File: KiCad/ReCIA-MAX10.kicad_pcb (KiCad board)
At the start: 4 copper layers, 17.4 x 51.4 mm, 18 parts, among them J1 Conn_02x03_Odd_Even, U1 AMS1117-3.3, U2 SN74CBT16210, U3 SN74CBT16210, U4 10M02SCU169, U5 8520_DIP_SOCKET, X1 Oscillator_3.2x2.5mm-28.6363M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

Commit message: more routing, pin assignments and silkscreen fixes
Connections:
- net Net-(U3-Pad25) renamed PA2_3V3
- net Net-(U3-Pad26) renamed PA1_3V3
- net Net-(U3-Pad27) renamed PA0_3V3
- net Net-(U3-Pad28) renamed PA3_3V3
- net Net-(U3-Pad29) renamed PA4_3V3
- net Net-(U3-Pad30) renamed PA5_3V3
- net Net-(U3-Pad31) renamed PA6_3V3
- net Net-(U3-Pad33) renamed PA7_3V3
- net Net-(U3-Pad36) renamed D2_3V3
- net Net-(U3-Pad37) renamed D1_3V3
- net Net-(U3-Pad38) renamed D0_3V3
- net Net-(U3-Pad39) renamed RESET_3V3
- net Net-(U3-Pad40) renamed A3_3V3
- net Net-(U3-Pad42) renamed A2_3V3
- net Net-(U3-Pad43) renamed CNT_3V3
- net Net-(U3-Pad44) renamed SP_3V3
- net Net-(U3-Pad45) renamed A0_3V3
- net Net-(U3-Pad46) renamed A1_3V3
- U3 pad 10: Net-(U3-Pad10) -> D0
- U3 pad 11: Net-(U3-Pad11) -> D1
- U3 pad 12: Net-(U3-Pad12) -> D2
- U3 pad 6: Net-(U3-Pad6) -> A2
- U3 pad 7: Net-(U3-Pad7) -> A3
- U3 pad 9: Net-(U3-Pad9) -> RESET
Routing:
- net D2: track 0.00 -> 18.1 mm
- net D1: track 0.00 -> 15.4 mm
- net D0: track 0.00 -> 12.7 mm
- net D2_3V3: track 0.00 -> 12.5 mm, vias 0 -> 1
- net D1_3V3: track 0.00 -> 12.1 mm, vias 0 -> 1
- net D0_3V3: track 0.00 -> 11.4 mm, vias 0 -> 1
- net RESET: track 0.00 -> 10.0 mm
- net A3: track 0.00 -> 7.34 mm
- net A2: track 0.00 -> 6.55 mm
- net RESET_3V3: track 0.00 -> 3.07 mm
- net A3_3V3: track 0.00 -> 2.82 mm
- net GND: vias 56 -> 58
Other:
- board text added: "1A"
- board text added: "8520"
- board text added: "ReCIA"
- board text added: "Rev."

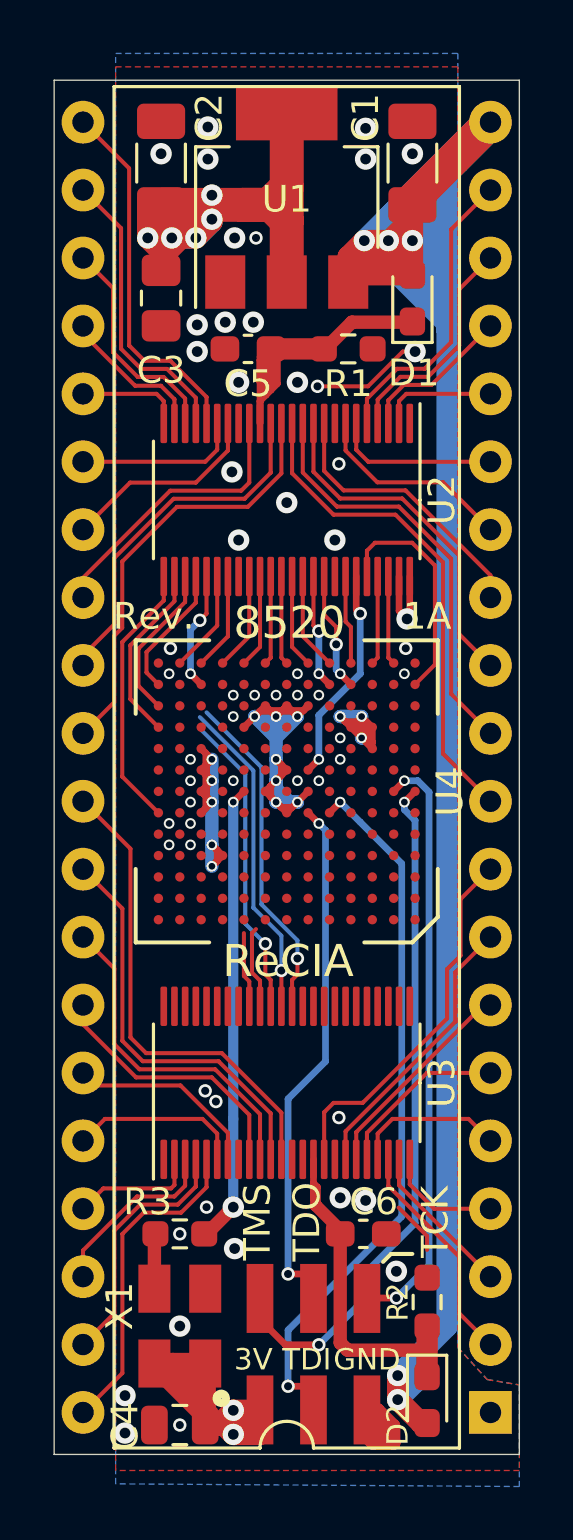
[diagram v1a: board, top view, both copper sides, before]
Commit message: more pin assignments and routing
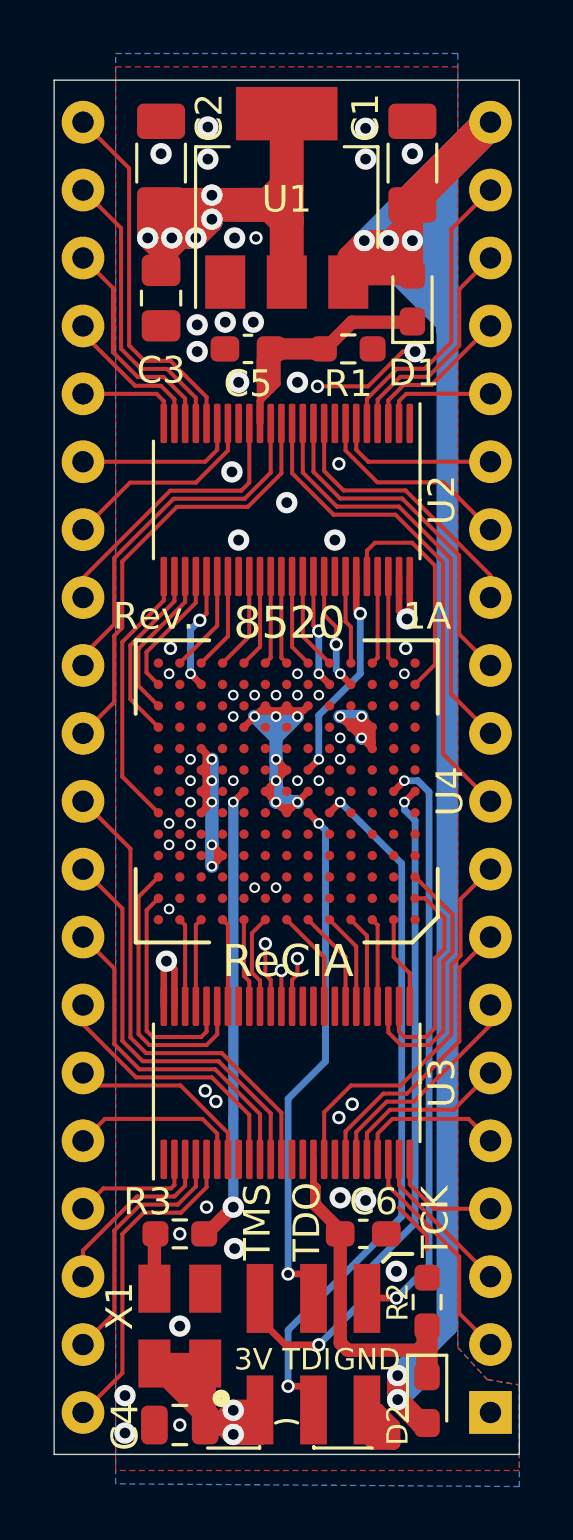
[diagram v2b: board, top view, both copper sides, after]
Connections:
- U3 pad 13: Net-(U3-Pad13) -> GND
- U3 pad 14: Net-(U3-Pad14) -> GND
- U4 pad A10: Net-(U4-PadA10) -> A2_3V3
- U4 pad A11: Net-(U4-PadA11) -> A0_3V3
- U4 pad A12: Net-(U4-PadA12) -> A1_3V3
- U4 pad A2: Net-(U4-PadA2) -> PA2_3V3
- U4 pad A3: Net-(U4-PadA3) -> PA3_3V3
- U4 pad A4: Net-(U4-PadA4) -> PA4_3V3
- U4 pad A5: Net-(U4-PadA5) -> PA5_3V3
- U4 pad A6: Net-(U4-PadA6) -> PA6_3V3
- U4 pad A7: Net-(U4-PadA7) -> PA7_3V3
- U4 pad A8: Net-(U4-PadA8) -> RESET_3V3
- U4 pad A9: Net-(U4-PadA9) -> A3_3V3
- U4 pad B1: Net-(U4-PadB1) -> PA1_3V3
- U4 pad B13: Net-(U4-PadB13) -> SP_3V3
- U4 pad C1: Net-(U4-PadC1) -> PA0_3V3
- U4 pad C13: Net-(U4-PadC13) -> CNT_3V3
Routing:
- net D1_3V3: track 12.1 -> 1.34 mm
- net D2_3V3: track 12.5 -> 1.87 mm
- net CNT_3V3: track 0.00 -> 10.5 mm
- net PA0_3V3: track 0.00 -> 9.93 mm
- net D0_3V3: track 11.4 -> 2.42 mm
- net SP_3V3: track 0.00 -> 8.50 mm
- net PA1_3V3: track 0.00 -> 8.18 mm
- net PA7_3V3: track 0.00 -> 3.82 mm
- net PA6_3V3: track 0.00 -> 3.82 mm
- net PA5_3V3: track 0.00 -> 3.65 mm
- net GND: track 15.8 -> 19.4 mm, vias 58 -> 63
- net PA4_3V3: track 0.00 -> 3.49 mm
- net PA2_3V3: track 0.00 -> 3.49 mm
- net PA3_3V3: track 0.00 -> 3.32 mm
- net A2_3V3: track 0.00 -> 3.32 mm
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
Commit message: more power routing, vias and silkscreen fixes
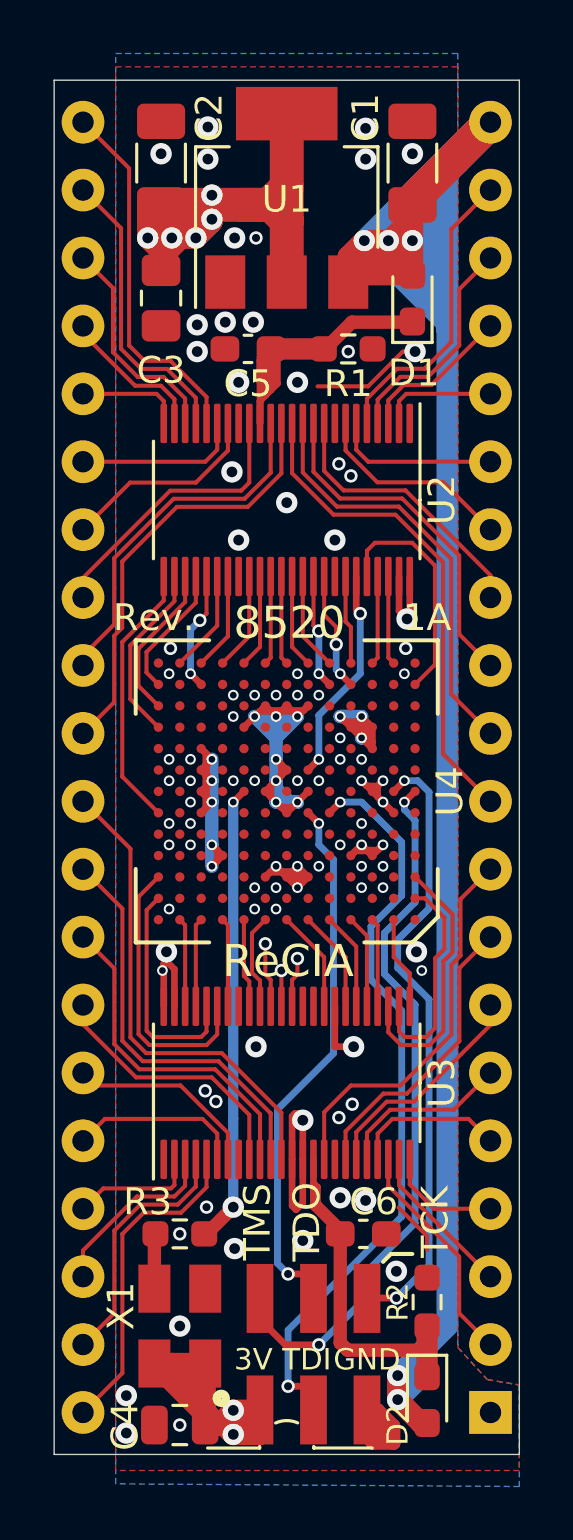
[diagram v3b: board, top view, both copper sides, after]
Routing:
- net 3V3: track 102.0 -> 116.7 mm, vias 22 -> 30
- net GND: track 19.4 -> 29.2 mm, vias 63 -> 84
- net TDI: track 26.9 -> 28.3 mm
- net TCK: track 22.2 -> 23.2 mm
- net TMS: track 25.9 -> 26.9 mm
- net TDO: track 19.9 -> 20.5 mm

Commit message: Changed to minimum width to 0.14 mm for front F.Cu zone and solid pad connection to zone for BGA-footprint.
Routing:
- net GND: vias 84 -> 85

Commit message: Silkscreen fixes, add dot indicator for pin 1 on U2,U3,U4
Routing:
- net PA1_3V3: track 8.18 -> 7.68 mm

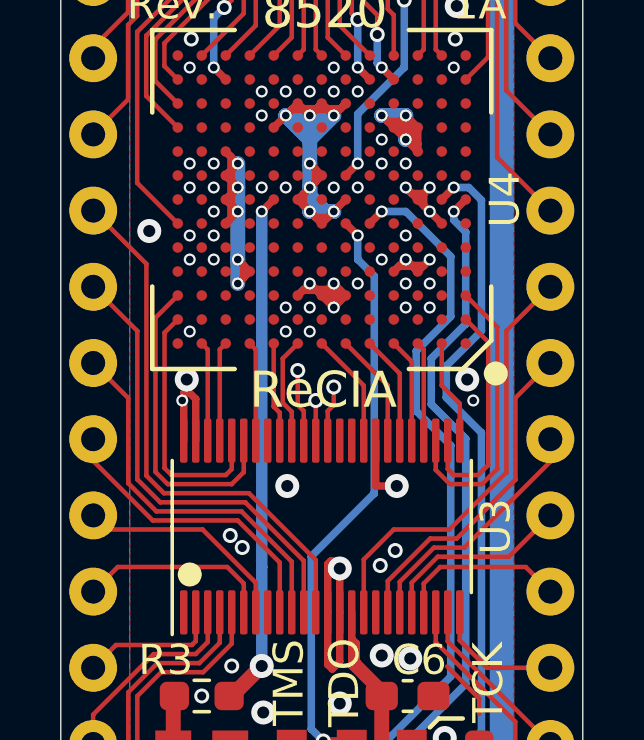
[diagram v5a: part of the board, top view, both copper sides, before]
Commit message: Add pin assignment and routing for D0,D1,D2 to the FPGA
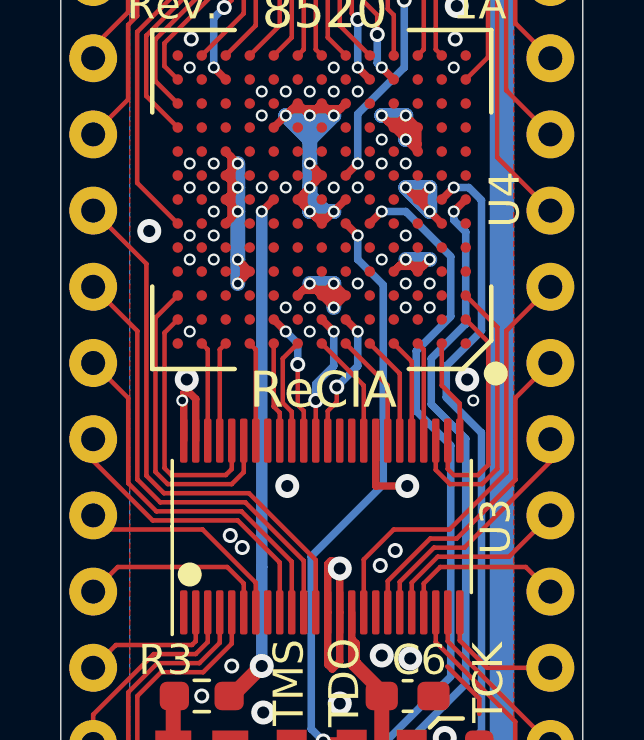
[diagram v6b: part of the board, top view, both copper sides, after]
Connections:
- U4 pad B6: Net-(U4-PadB6) -> D2_3V3
- U4 pad B7: Net-(U4-PadB7) -> D1_3V3
- U4 pad B9: Net-(U4-PadB9) -> D0_3V3
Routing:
- net 3V3: track 116.7 -> 121.9 mm
- net D1_3V3: track 1.34 -> 4.45 mm, vias 1 -> 2
- net D2_3V3: track 1.87 -> 4.62 mm, vias 1 -> 2
- net D0_3V3: track 2.42 -> 4.45 mm, vias 1 -> 2
- net GND: vias 85 -> 84

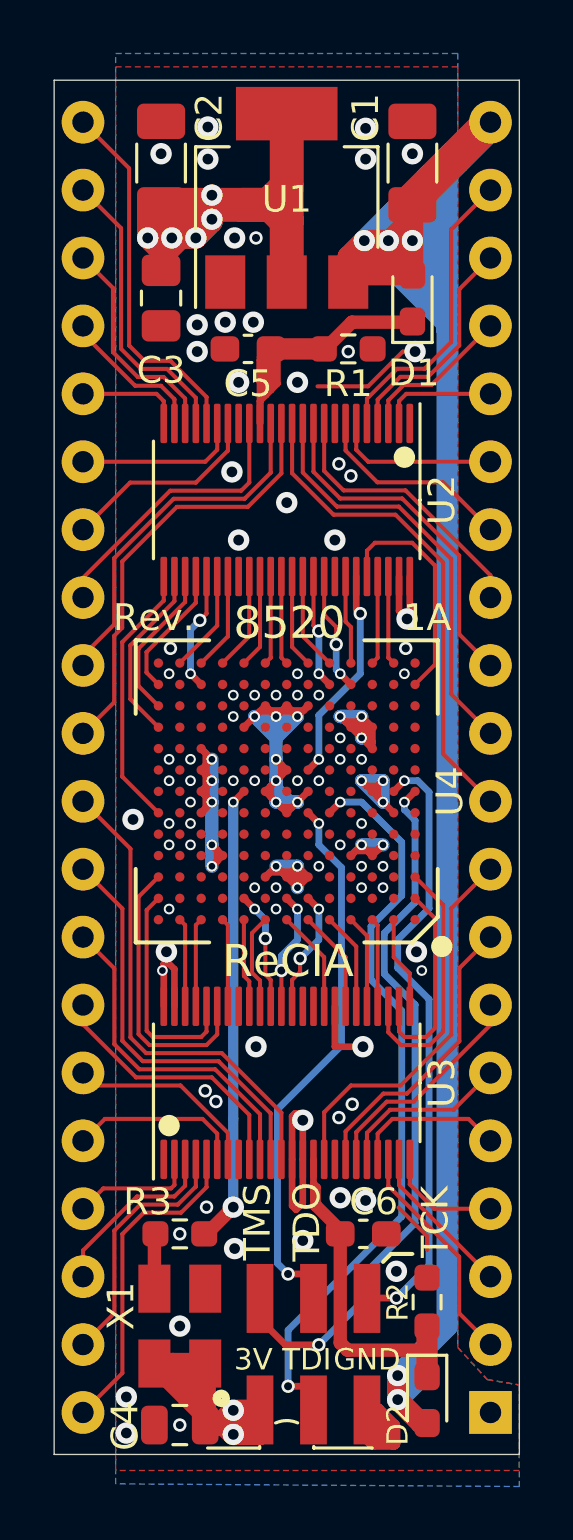
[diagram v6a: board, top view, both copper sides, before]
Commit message: Add decoupling caps for FPGA-chip
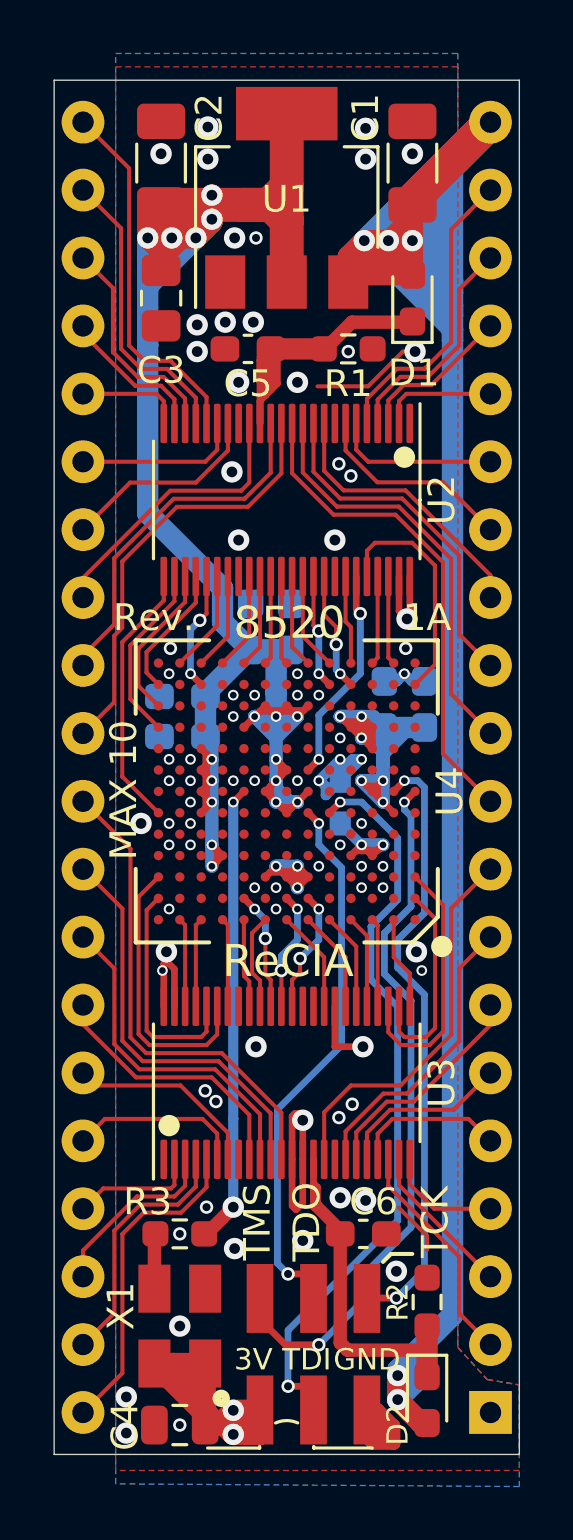
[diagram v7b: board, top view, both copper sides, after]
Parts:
- added C10: 0.1uF, Capacitor_SMD:C_0603_1608Metric_Pad1.08x0.95mm_HandSolder, B.Cu at (130.7, 77.8)
- added C11: 0.1uF, Capacitor_SMD:C_0603_1608Metric_Pad1.08x0.95mm_HandSolder, B.Cu at (135.7, 80.7)
- added C12: 0.1uF, Capacitor_SMD:C_0603_1608Metric_Pad1.08x0.95mm_HandSolder, B.Cu at (137.2, 80.7)
- added C13: 0.1uF, Capacitor_SMD:C_0603_1608Metric_Pad1.08x0.95mm_HandSolder, B.Cu at (134.0, 84.3)
- added C7: 0.1uF, Capacitor_SMD:C_0603_1608Metric_Pad1.08x0.95mm_HandSolder, B.Cu at (128.1, 80.3)
- added C8: 0.1uF, Capacitor_SMD:C_0603_1608Metric_Pad1.08x0.95mm_HandSolder, B.Cu at (128.1, 81.8)
- added C9: 0.1uF, Capacitor_SMD:C_0603_1608Metric_Pad1.08x0.95mm_HandSolder, B.Cu at (132.2, 77.8)
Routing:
- net 3V3: track 121.9 -> 168.9 mm
- net GND: track 29.2 -> 36.0 mm, vias 84 -> 82
- net VCC: track 95.1 -> 100.3 mm
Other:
- board text added: "MAX 10"

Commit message: Add more decoupling caps for FPGA-chip
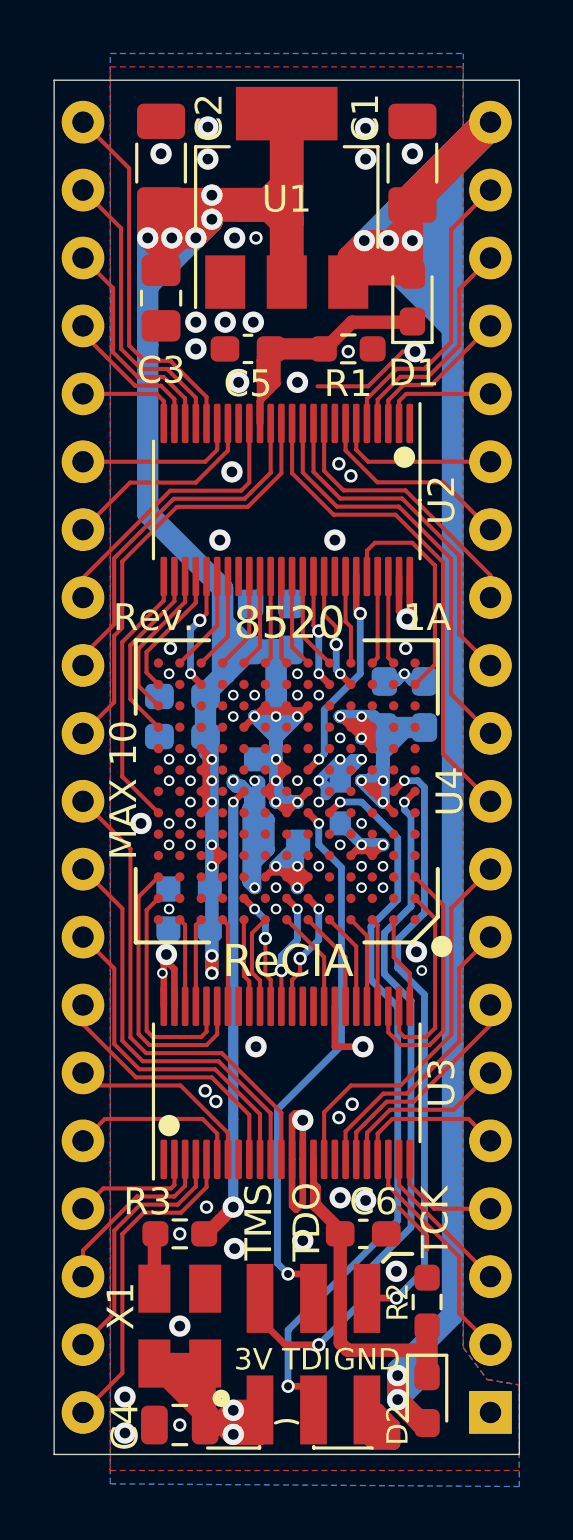
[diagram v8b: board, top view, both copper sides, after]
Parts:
- added C13: 0.01uF, Capacitor_SMD:C_0603_1608Metric_Pad1.08x0.95mm_HandSolder, B.Cu at (130.8, 83.5)
- added C16: 0.01uF, Capacitor_SMD:C_0603_1608Metric, B.Cu at (131.7, 85.8)
- added C17: 0.01uF, Capacitor_SMD:C_0603_1608Metric, B.Cu at (128.3, 87.5)
- added C7: 0.1uF, Capacitor_SMD:C_0603_1608Metric_Pad1.08x0.95mm_HandSolder, B.Cu at (130.7, 77.8)
- C10: footprint Capacitor_SMD:C_0603_1608Metric_Pad1.08x0.95mm_HandSolder -> Capacitor_SMD:C_0603_1608Metric
- C11: renamed from C9; value 0.1uF -> 0.01uF
- C12: renamed from C11; value 0.1uF -> 0.01uF
- C14: renamed from C8; value 0.1uF -> 0.01uF
- C15: renamed from C13; value 0.1uF -> 0.01uF
- moved C10 11.5 mm to (128.3, 89.0), turned to 180 degrees
- renumbered C12 to C8, C7 to C9
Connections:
- net XTAL_28M renamed XTAL_CLK
- U4 pad G5: Net-(U4-PadG5) -> GND
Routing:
- net 3V3: track 168.9 -> 184.4 mm, vias 30 -> 32
- net GND: track 36.0 -> 46.6 mm, vias 82 -> 83
